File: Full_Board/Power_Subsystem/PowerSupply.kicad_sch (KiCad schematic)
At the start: 10 parts, among them J7 KLDHCX-8-0202-A, U1 LM2576SX-3.3-NOPB

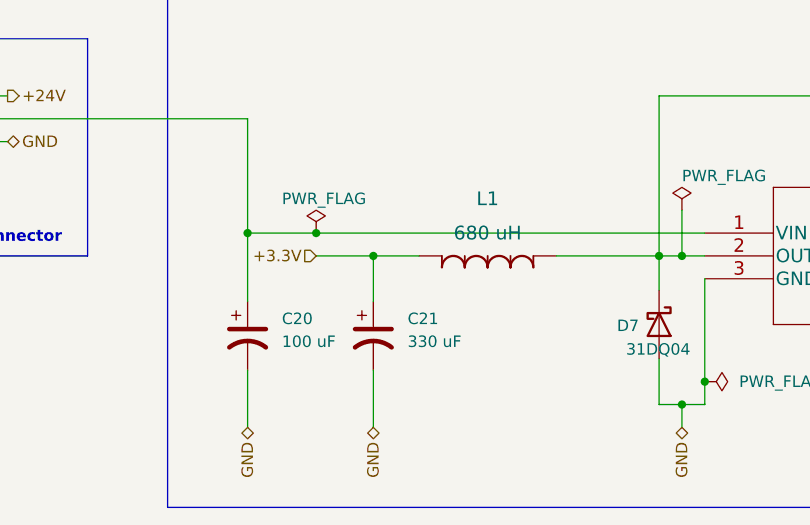
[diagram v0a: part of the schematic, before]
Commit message: Fix annotations, add test points
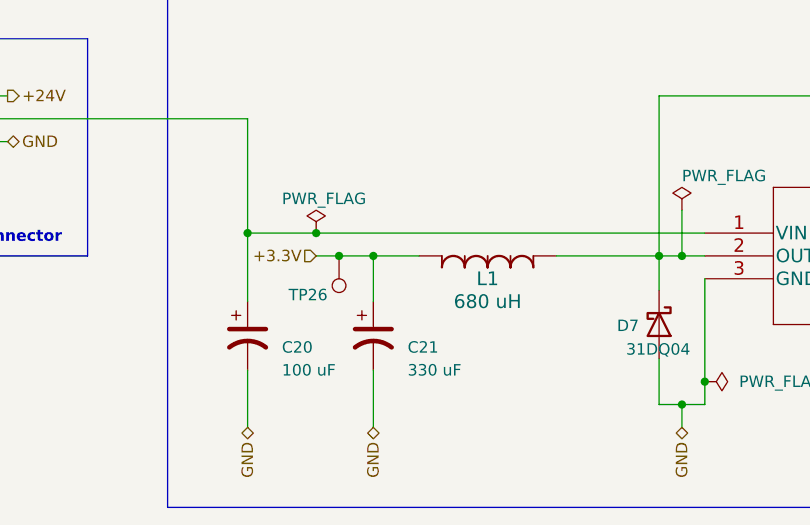
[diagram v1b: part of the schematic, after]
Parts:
- added TP26: ~, TestPoint:TestPoint_Keystone_5010-5014_Multipurpose, symbol Connector:TestPoint
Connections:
- net +3.3V: now also TP26.1
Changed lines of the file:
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@@
   (junction (at 96.52 82.55) (diameter 0) (color 0 0 0 0)
+  )
+  (junction (at 135.89 95.25) (diameter 0) (color 0 0 0 0)
   )
   (junction (at 139.7 95.25) (diameter 0) (color 0 0 0 0)
@@
     (stroke (width 0) (type default) (color 0 0 0 0))
   )
-  (wire (pts (xy 133.35 95.25) (xy 139.7 95.25))
+  (wire (pts (xy 133.35 95.25) (xy 135.89 95.25))
     (stroke (width 0) (type default) (color 0 0 0 0))
   )
@@
   )
   (polyline (pts (xy 107.95 95.25) (xy 62.23 95.25))
+    (stroke (width 0) (type default) (color 0 0 0 0))
+  )
+  (wire (pts (xy 135.89 95.25) (xy 139.7 95.25))
     (stroke (width 0) (type default) (color 0 0 0 0))
   )
@@
   )
   (symbol (lib_id "Device:C_Polarized_US") (at 125.73 104.14 0) (unit 1)
-    (in_bom yes) (on_board yes) (fields_autoplaced)
-    (property "Reference" "C20" (id 0) (at 129.54 102.2349 0)
-      (effects (font (size 1.27 1.27)) (justify left))
-    )
-    (property "Value" "100 uF" (id 1) (at 129.54 104.7749 0)
+    (in_bom yes) (on_board yes)
+    (property "Reference" "C20" (id 0) (at 129.54 105.41 0)
+      (effects (font (size 1.27 1.27)) (justify left))
+    )
+    (property "Value" "100 uF" (id 1) (at 129.54 107.95 0)
       (effects (font (size 1.27 1.27)) (justify left))
     )
@@
   )
   (symbol (lib_id "SRR1210-681M:SRR1210-681M") (at 160.02 95.25 180) (unit 1)
-    (in_bom yes) (on_board yes) (fields_autoplaced)
-    (property "Reference" "L1" (id 0) (at 152.4 88.9 0)
+    (in_bom yes) (on_board yes)
+    (property "Reference" "L1" (id 0) (at 152.4 97.79 0)
       (effects (font (size 1.524 1.524)))
     )
-    (property "Value" "680 uH" (id 1) (at 152.4 92.71 0)
+    (property "Value" "680 uH" (id 1) (at 152.4 100.33 0)
       (effects (font (size 1.524 1.524)))
     )
@@
   )
   (symbol (lib_id "Device:C_Polarized_US") (at 139.7 104.14 0) (unit 1)
-    (in_bom yes) (on_board yes) (fields_autoplaced)
-    (property "Reference" "C21" (id 0) (at 143.51 102.2349 0)
-      (effects (font (size 1.27 1.27)) (justify left))
-    )
-    (property "Value" "330 uF" (id 1) (at 143.51 104.7749 0)
+    (in_bom yes) (on_board yes)
+    (property "Reference" "C21" (id 0) (at 143.51 105.41 0)
+      (effects (font (size 1.27 1.27)) (justify left))
+    )
+    (property "Value" "330 uF" (id 1) (at 143.51 107.95 0)
       (effects (font (size 1.27 1.27)) (justify left))
     )
@@
       (effects (font (size 1.27 1.27)) hide)
     )
+    (pin "1")
+  )
+  (symbol (lib_id "Connector:TestPoint") (at 135.89 95.25 180) (unit 1)
+    (in_bom yes) (on_board yes)
+    (property "Reference" "TP26" (id 0) (at 134.62 100.33 0)
+      (effects (font (size 1.27 1.27)) (justify left top))
+    )
+    (property "Value" "~" (id 1) (at 133.35 97.2821 0)
+      (effects (font (size 1.27 1.27)) (justify left) hide)
+    )
+    (property "Footprint" "TestPoint:TestPoint_Keystone_5010-5014_Multipurpose" (id 2) (at 130.81 95.25 0)
+      (effects (font (size 1.27 1.27)) hide)
+    )
+    (property "Datasheet" "~" (id 3) (at 130.81 95.25 0)
+      (effects (font (size 1.27 1.27)) hide)
+    )
+    (property "Mouser link" "https://www.mouser.com/ProductDetail/Keystone-Electronics/5010?qs=qOqV1E1P08SzD%252BWfk1wMXQ%3D%3D" (id 4) (at 135.89 95.25 0)
+      (effects (font (size 1.27 1.27)) hide)
+    )
+    (property "Digikey Part Number" "36-5010-ND" (id 5) (at 135.89 95.25 0)
+      (effects (font (size 1.27 1.27)) hide)
+    )
+    (property "Digikey link" "https://www.digikey.com/en/products/detail/keystone-electronics/5010/255332?s=N4IgTCBcDaIKwAYCMCQF0C%2BQhttps://www.digikey.com/en/products/detail/keystone-electronics/5010/255332?s=N4IgTCBcDaIKwAYCMCQF0C%2BQ" (id 6) (at 135.89 95.25 0)
+      (effects (font (size 1.27 1.27)) hide)
+    )
+    (property "Manufacturer's Part Number" "5010" (id 7) (at 135.89 95.25 0)
+      (effects (font (size 1.27 1.27)) hide)
+    )
+    (property "Mouser Part Number" "534-5010" (id 8) (at 135.89 95.25 0)
+      (effects (font (size 1.27 1.27)) hide)
+    )

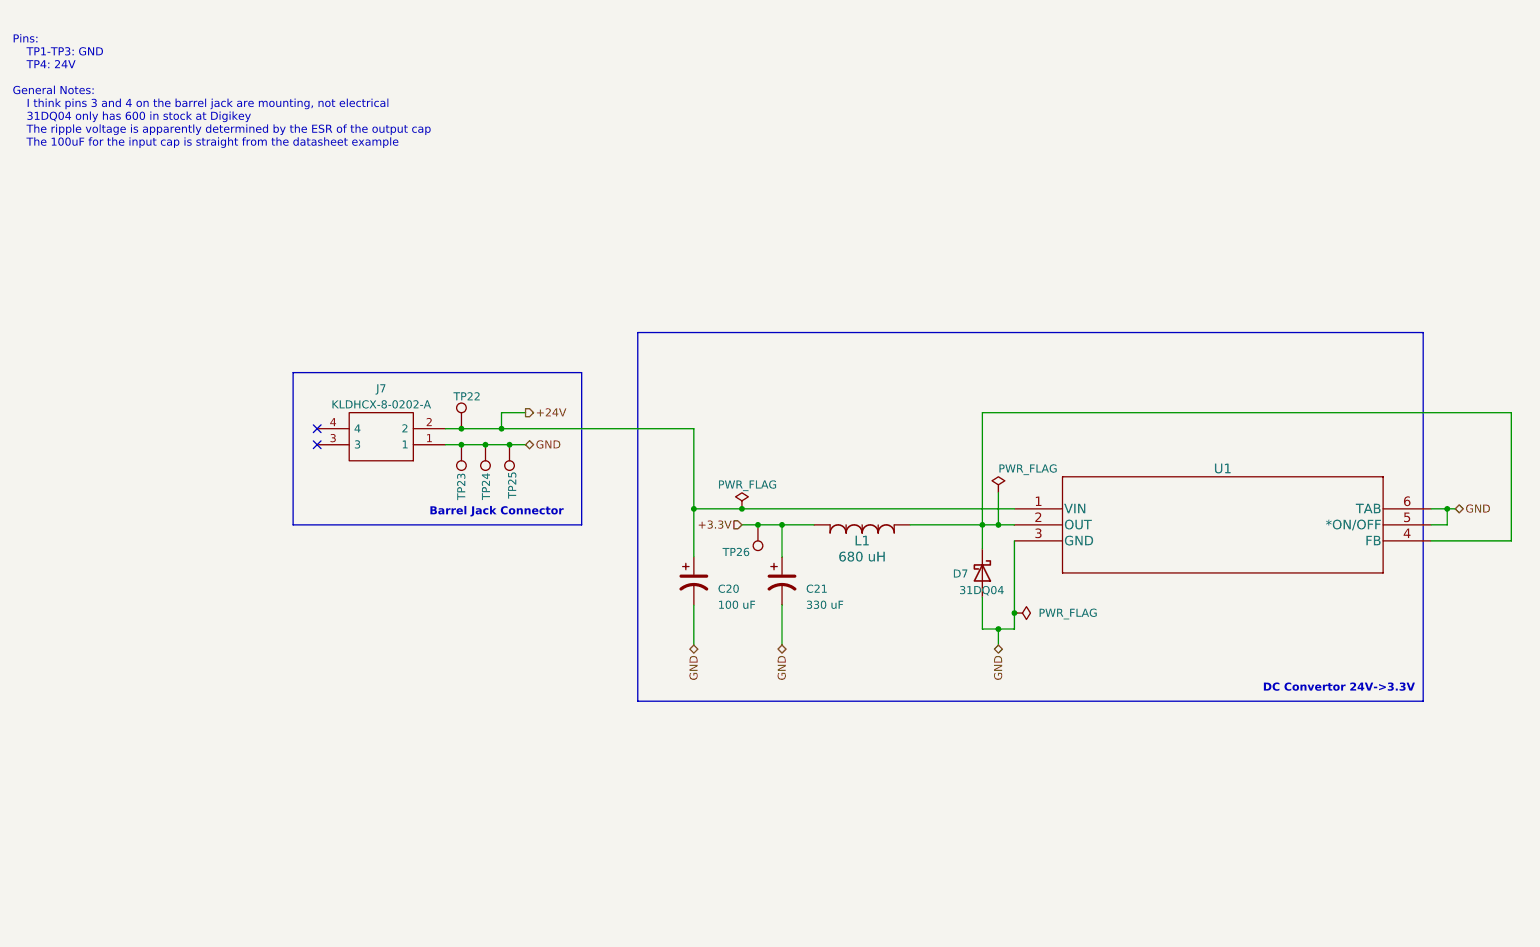
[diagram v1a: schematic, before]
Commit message: Add screenshots of each subsystem
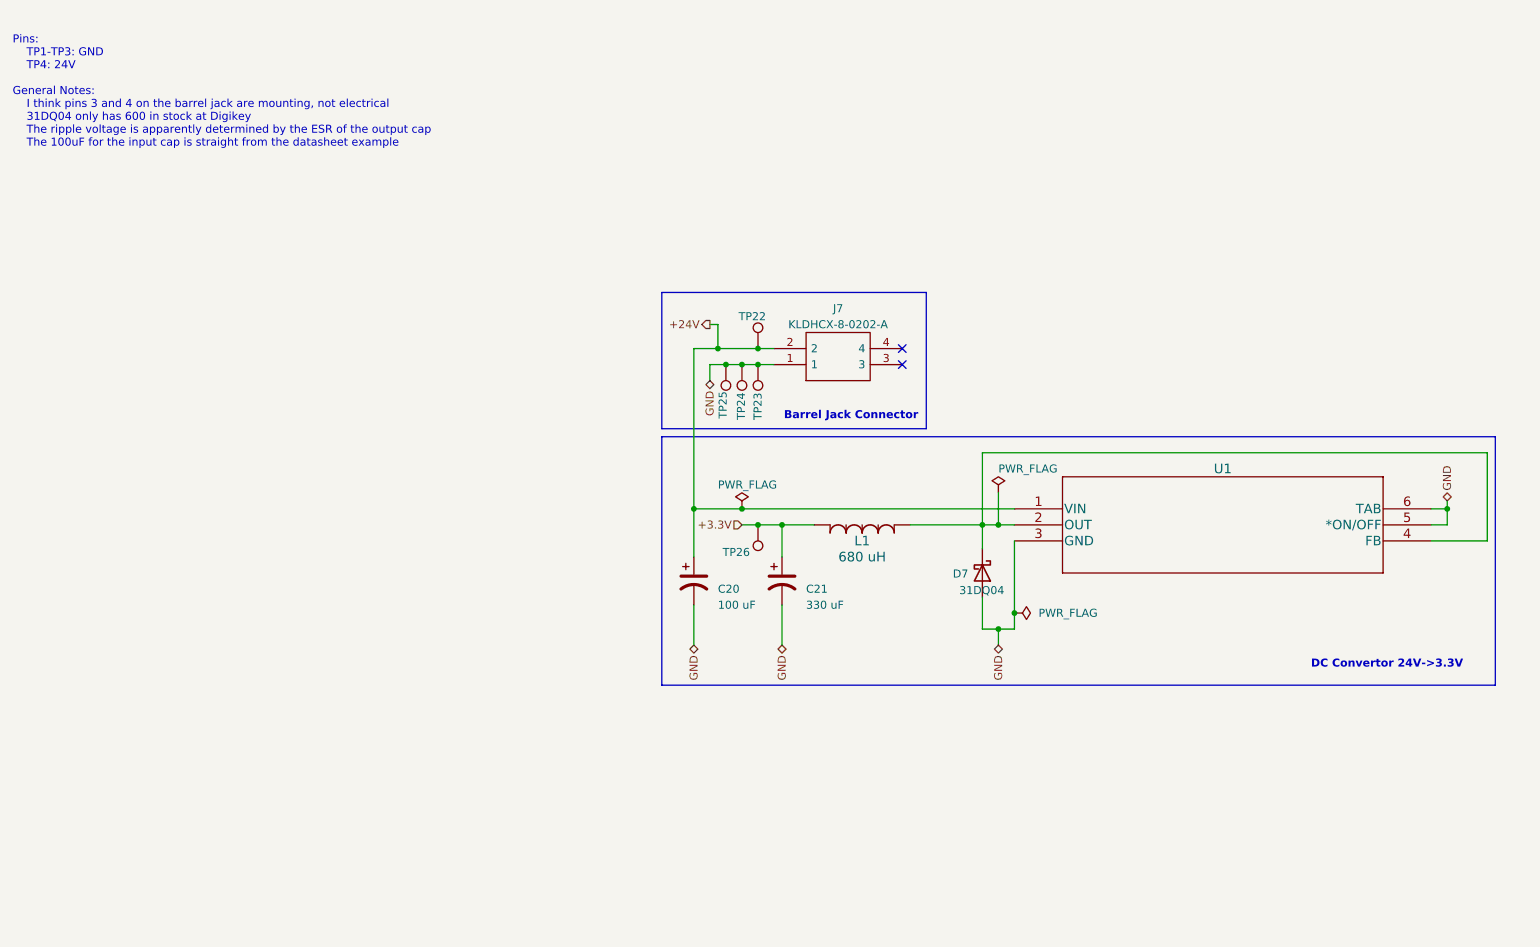
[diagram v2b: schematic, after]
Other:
- moved on the sheet: J7, TP22, TP23, TP24, TP25

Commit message: Added 5V power supply
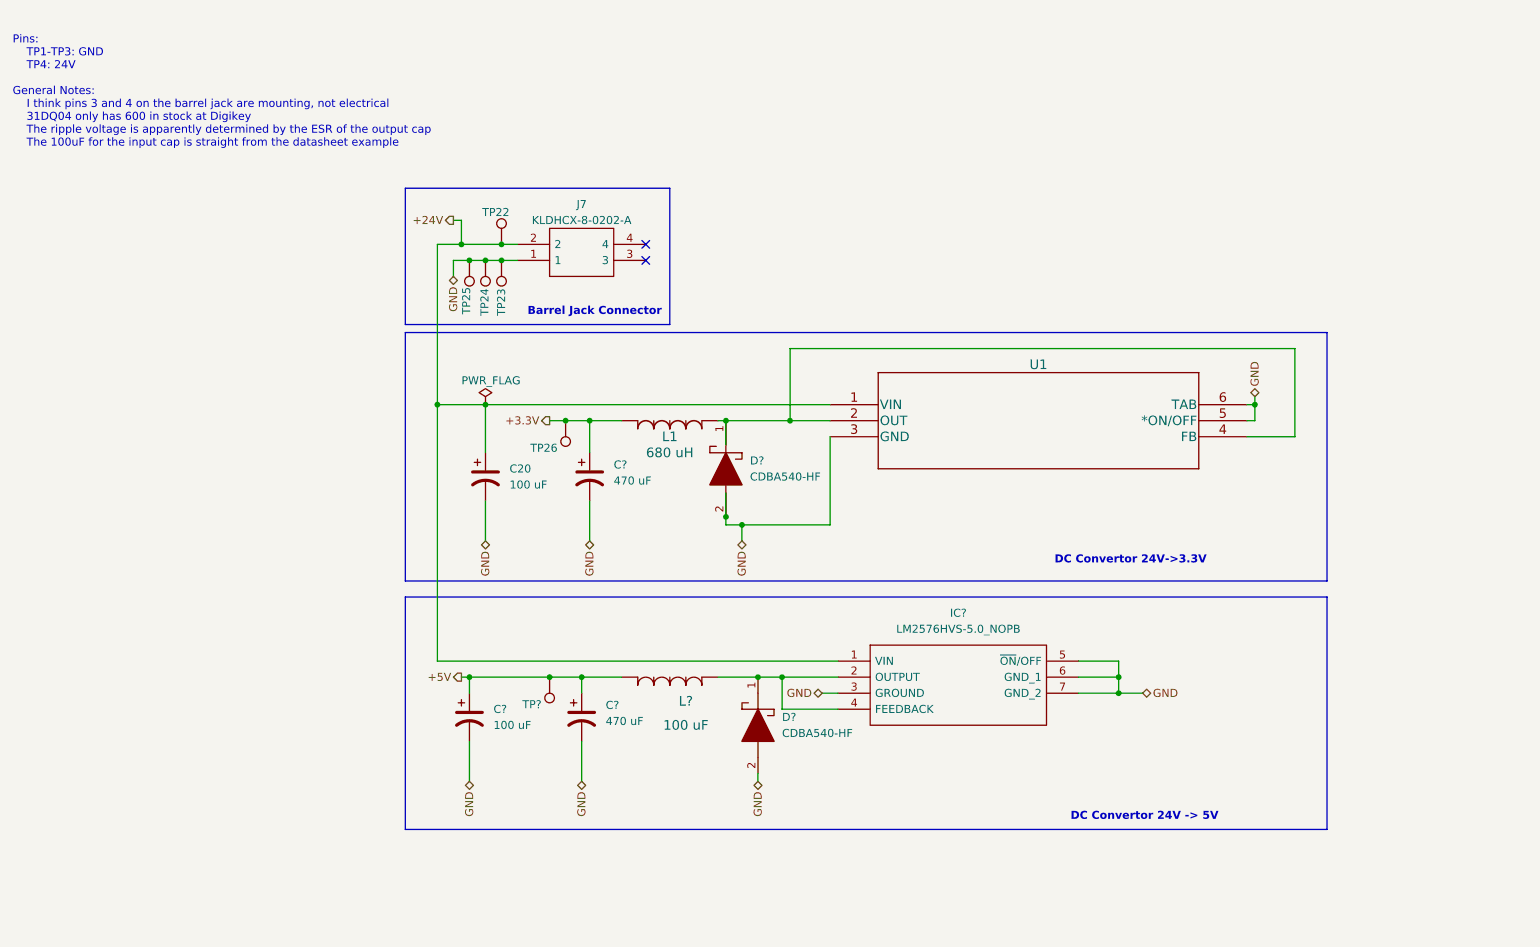
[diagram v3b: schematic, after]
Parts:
- removed C21: 330 uF, Capacitor_THT:CP_Radial_D10.0mm_P5.00mm, symbol Device:C_Polarized_US
- removed D7: 31DQ04, Diode_THT:D_DO-201AD_P15.24mm_Horizontal, symbol Device:D_Schottky
- added C? (x2): 470 uF, symbol Device:C_Polarized_US
- added C?: 100 uF, Capacitor_THT:C_Radial_D6.3mm_H5.0mm_P2.50mm, symbol Device:C_Polarized_US
- added D? (x2): CDBA540-HF, DIOM5225X250N, symbol CDBA540-HF:CDBA540-HF
- added IC?: LM2576HVS-5.0_NOPB, LM2576HVS50NOPB, symbol LM25766HVS-5.0_NOPB:LM2576HVS-5.0_NOPB
- added L?: 100 uF, IND_44.104NLT_PUL, symbol PA4344-104NLT:PA4344.104NLT
- added TP?: ~, TestPoint:TestPoint_Keystone_5010-5014_Multipurpose, symbol Connector:TestPoint
- C20: footprint Capacitor_SMD:CP_Elec_3x5.3 -> Capacitor_THT:C_Radial_D6.3mm_H5.0mm_P2.50mm
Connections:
- net +24V: now also IC?.1 (VIN)
- net +3.3V: now also C?.1
- net GND: now also C?.2, C?.2, C?.2, D?.2, D?.2, IC?.3 (GROUND), IC?.5 (~{ON}/OFF), IC?.6 (GND_1), IC?.7 (GND_2)
- net at L1.2, U1.2 (OUT), U1.4 (FB): now also D?.1
- new net: D?.1, IC?.2 (OUTPUT), IC?.4 (FEEDBACK), L?.2
- new net +5V: C?.1, C?.1, L?.1, TP?.1
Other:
- note added: "DC Convertor 24V -> 5V"
- moved on the sheet: C20, J7, L1, TP22, TP23, TP24, TP25, TP26, U1

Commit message: Added extra bypass caps to the power supply
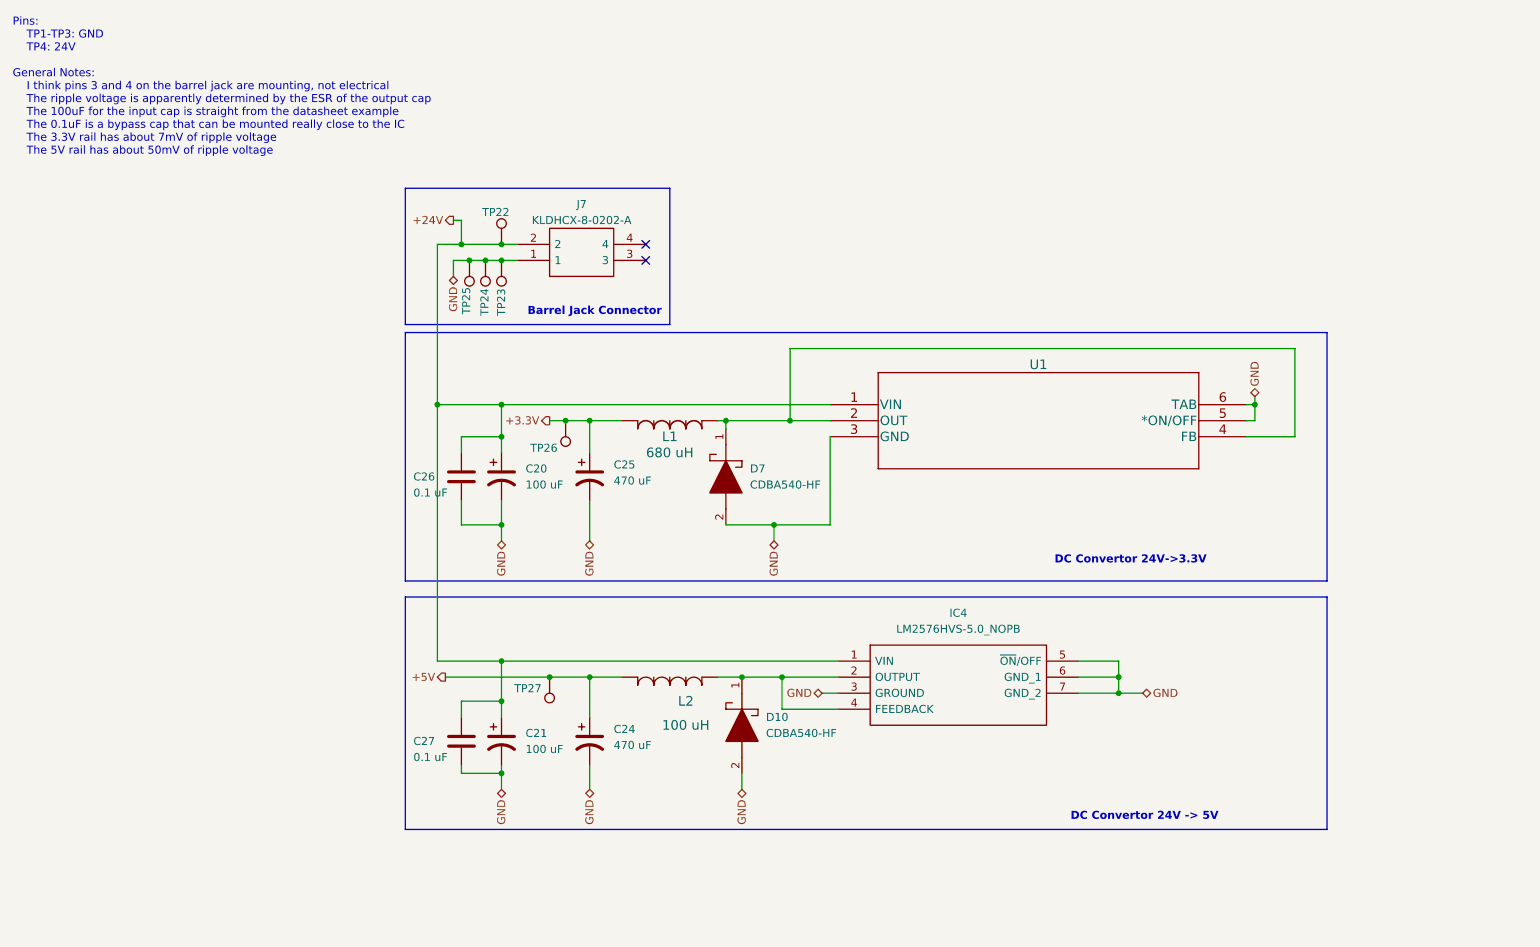
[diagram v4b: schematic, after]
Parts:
- removed D?: CDBA540-HF, DIOM5225X250N, symbol CDBA540-HF:CDBA540-HF
- added C26, C27: 0.1 uF, CL05A104KP5NNNC:CL05A104KP5NNNC, symbol Device:C
- added D7: CDBA540-HF, CDBA540-HF:DIOM5225X250N, symbol CDBA540-HF:CDBA540-HF
- C24, C25: renamed from C?; footprint (none) -> EEE-FP1E471AP:EEE-FP1E471AP; Digikey Part Number PCE4440CT-ND -> PCE4440DKR-ND
- D10: renamed from D?; footprint DIOM5225X250N -> CDBA540-HF:DIOM5225X250N; Digikey Link (none) -> https://www.digikey.com/en/products/detail/comchip-technolo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; Digikey Part Number (none) -> 641-1707-1-ND
- L2: renamed from L?; value 100 uF -> 100 uH; Digikey Link (none) -> https://www.digikey.com/en/products/detail/pulse-electronic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; Digikey Part Number (none) -> 553-3011-1-ND; Manufacturers Part Number (none) -> PA4344.104NLT
- gave numbers to parts that had none: 3
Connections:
- net +24V: now also C21.1, C26.1, C27.1
- net +5V: no longer C21.1
- net GND: now also C26.2, C27.2, D7.2
- net at L1.2, U1.2 (OUT), U1.4 (FB): now also D7.1
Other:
- note added: "Pins: TP1-TP3: GND TP4: 24V General Notes: I think pins 3 and 4 on the barrel jack are mounting, not electrical The ripple voltage is apparently determined by the ESR of the output cap The 100uF for the input cap is straight from the datasheet example The 0.1uF is a bypass cap that can be mounted really close to the IC The 3.3V rail has about 7mV of ripple voltage The 5V rail has about 50mV of ri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"
- note removed: "Pins: TP1-TP3: GND TP4: 24V General Notes: I think pins 3 and 4 on the barrel jack are mounting, not electrical 31DQ04 only has 600 in stock at Digikey The ripple voltage is apparently determined by the ESR of the output cap The 100uF for the input cap is straight from the datasheet example"
- moved on the sheet: C20, C21, C24, D10
